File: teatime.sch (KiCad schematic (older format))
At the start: 85 parts, among them SW1 SW_Push, U1 MCP1700-3302E_TO92, U2 74HC595, U3 74HC595, U4 74HC595, U5 74HC595, U6 ATtiny85-20PU

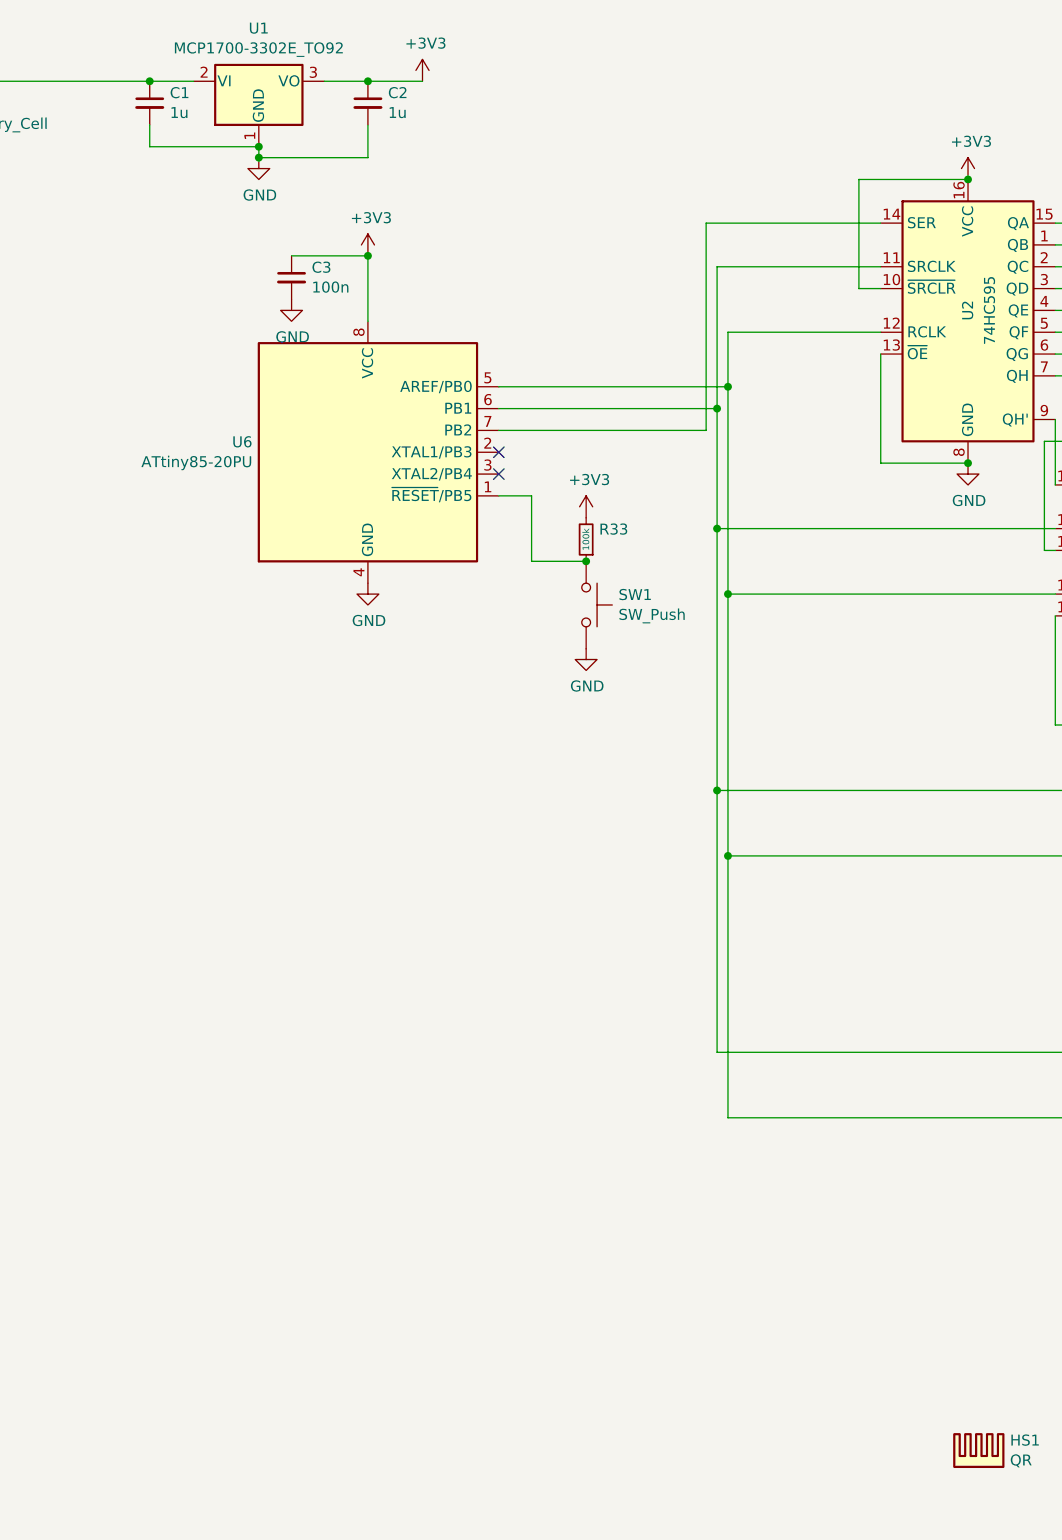
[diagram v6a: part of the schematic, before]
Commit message: More updates, added buzzer
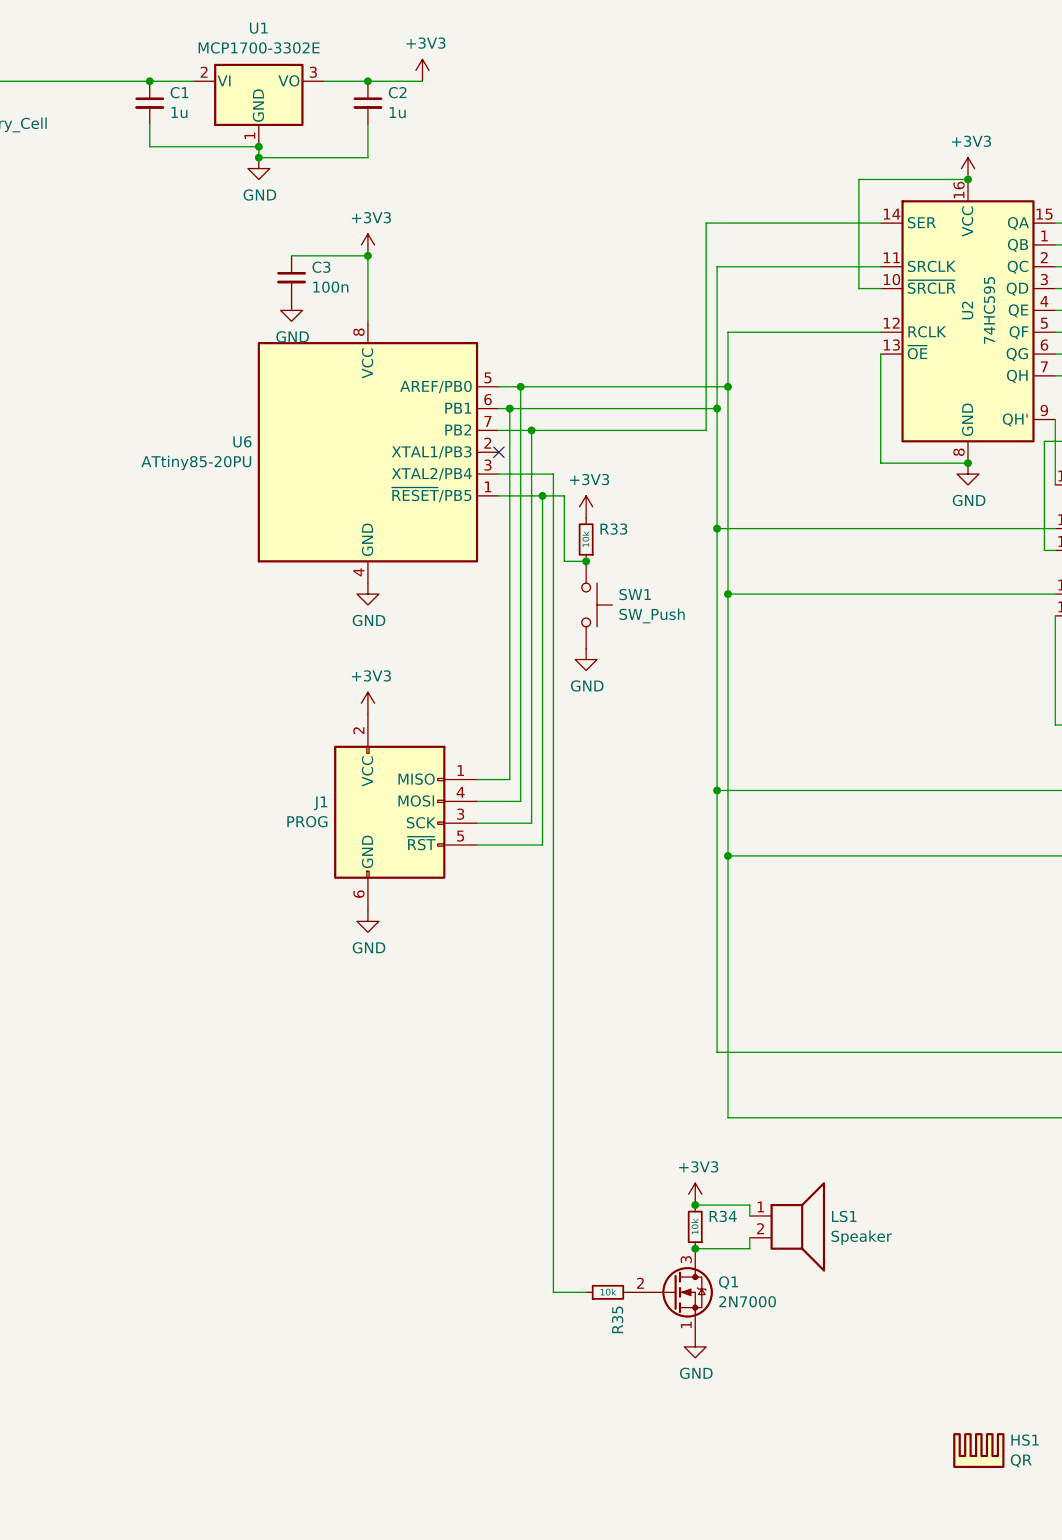
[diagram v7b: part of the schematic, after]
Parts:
- added J1: PROG, Connector_PinHeader_2.54mm:PinHeader_2x03_P2.54mm_Vertical, symbol Connector:AVR-ISP-6
- added LS1: Speaker, Buzzer_Beeper:Buzzer_12x9.5RM7.6, symbol Device:Speaker
- added Q1: 2N7000, Package_TO_SOT_THT:TO-92_Inline_W4.0mm_Horizontal_FlatSideDown, symbol Transistor_FET:2N7000
- added R34, R35: 10k, Resistor_THT:R_Axial_DIN0204_L3.6mm_D1.6mm_P7.62mm_Horizontal, symbol Device:R_Small
- R33: value 100k -> 10k
- U1: value MCP1700-3302E_TO92 -> MCP1700-3302E
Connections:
- net +3V3: now also J1.2 (VCC), LS1.1, R34.2
- net GND: now also J1.6 (GND), Q1.1 (S)
- net at U2.11 (SRCLK), U3.11 (SRCLK), U4.11 (SRCLK)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: now also J1.1 (MISO)
- net at U2.12 (RCLK), U3.12 (RCLK), U4.12 (RCLK)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: now also J1.4 (MOSI)
- net at U2.14 (SER), U6.7 (PB2): now also J1.3 (SCK)
- net at R33.1, SW1.1, U6.1 (~RESET~/PB5): now also J1.5 (~RST)
- net at U6.3 (XTAL2/PB4): now also R35.1
- new net: LS1.2, Q1.3 (D), R34.1
- new net: Q1.2 (G), R35.2
- no-connect marks 3 -> 2
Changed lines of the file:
@@
 P 3700 3000
 F 0 "R33" H 3641 2954 50  0000 R CNN
-F 1 "100k" V 3700 3000 30  0000 C CNN
+F 1 "10k" V 3700 3000 30  0000 C CNN
 F 2 "Resistor_THT:R_Axial_DIN0204_L3.6mm_D1.6mm_P7.62mm_Horizontal" H 3700 3000 50  0001 C CNN
 F 3 "~" H 3700 3000 50  0001 C CNN
@@
 $EndComp
 Wire Wire Line
-	3300 2800 3450 2800
-Wire Wire Line
-	3450 2800 3450 3100
-Wire Wire Line
-	3450 3100 3700 3100
+	3300 2800 3500 2800
+Wire Wire Line
+	3600 2800 3600 3100
+Wire Wire Line
+	3600 3100 3700 3100
 Connection ~ 3700 3100
 Wire Wire Line
-	3300 2400 4300 2400
+	3300 2400 3350 2400
 $Comp
 L Regulator_Linear:MCP1700-3302E_TO92 U1
@@
 P 2200 900
 F 0 "U1" H 2200 658 50  0000 C CNN
-F 1 "MCP1700-3302E_TO92" H 2200 749 50  0000 C CNN
+F 1 "MCP1700-3302E" H 2200 749 50  0000 C CNN
 F 2 "Package_TO_SOT_THT:TO-92_Inline_W4.0mm_Horizontal_FlatSideDown" H 2200 700 50  0001 C CIN
 F 3 "http://ww1.microchip.com/downloads/en/DeviceDoc/20001826D.pdf" H 2200 900 50  0001 C CNN
@@
 Connection ~ 2200 1200
 NoConn ~ 3300 2600
-NoConn ~ 3300 2700
 $Comp
 L Device:R_Small R2
@@
 	4350 2300 4350 3250
 Wire Wire Line
-	3300 2300 4350 2300
+	3300 2300 3400 2300
 Wire Wire Line
 	4250 1550 4250 2500
 Wire Wire Line
-	4250 2500 3300 2500
+	4250 2500 3450 2500
 Wire Wire Line
 	9050 1200 9400 1200
@@
 Connection ~ 700  900
 Connection ~ 700  1200
+$Comp
+L Connector:AVR-ISP-6 J1
+U 1 1 5E4866F5
+P 2800 4300
+F 0 "J1" H 2520 4396 50  0000 R CNN
+F 1 "PROG" H 2520 4305 50  0000 R CNN
+F 2 "Connector_PinHeader_2.54mm:PinHeader_2x03_P2.54mm_Vertical" V 2550 4350 50  0001 C CNN
+F 3 " ~" H 1525 3750 50  0001 C CNN
+	1    2800 4300
+	1    0    0    -1
+$EndComp
+$Comp
+L power:+3V3 #PWR0101
+U 1 1 5E4868CF
+P 2700 3800
+F 0 "#PWR0101" H 2700 3650 50  0001 C CNN
+F 1 "+3V3" H 2715 3973 50  0000 C CNN
+F 2 "" H 2700 3800 50  0001 C CNN
+F 3 "" H 2700 3800 50  0001 C CNN
+	1    2700 3800
+	1    0    0    -1
+$EndComp
+$Comp
+L power:GND #PWR0102
+U 1 1 5E486986
+P 2700 4700
+F 0 "#PWR0102" H 2700 4450 50  0001 C CNN
+F 1 "GND" H 2705 4527 50  0000 C CNN
+F 2 "" H 2700 4700 50  0001 C CNN
+F 3 "" H 2700 4700 50  0001 C CNN
+	1    2700 4700
+	1    0    0    -1
+$EndComp
+Wire Wire Line
+	3200 4100 3350 4100
+Wire Wire Line
+	3200 4200 3400 4200
+Wire Wire Line
+	3200 4300 3450 4300
+Wire Wire Line
+	3200 4400 3500 4400
+Wire Wire Line
+	3500 4400 3500 2800
+Connection ~ 3500 2800
+Wire Wire Line
+	3500 2800 3600 2800
+Wire Wire Line
+	3450 2500 3450 4300
+Connection ~ 3450 2500
+Wire Wire Line
+	3450 2500 3300 2500
+Wire Wire Line
+	3400 2300 3400 4200
+Connection ~ 3400 2300
+Wire Wire Line
+	3400 2300 4350 2300
+Wire Wire Line
+	3350 2400 3350 4100
+Connection ~ 3350 2400
+Wire Wire Line
+	3350 2400 4300 2400
+$Comp
+L Device:Speaker LS1
+U 1 1 5E4D2D09
+P 4650 6100
+F 0 "LS1" H 4820 6096 50  0000 L CNN
+F 1 "Speaker" H 4820 6005 50  0000 L CNN
+F 2 "Buzzer_Beeper:Buzzer_12x9.5RM7.6" H 4650 5900 50  0001 C CNN
+F 3 "~" H 4640 6050 50  0001 C CNN
+	1    4650 6100
+	1    0    0    -1
+$EndComp
+$Comp
+L Transistor_FET:2N7000 Q1
+U 1 1 5E4D2E2E
+P 4100 6450
+F 0 "Q1" H 4305 6496 50  0000 L CNN
+F 1 "2N7000" H 4305 6405 50  0000 L CNN
+F 2 "Package_TO_SOT_THT:TO-92_Inline_W4.0mm_Horizontal_FlatSideDown" H 4300 6375 50  0001 L CIN
+F 3 "https://www.fairchildsemi.com/datasheets/2N/2N7000.pdf" H 4100 6450 50  0001 L CNN
+	1    4100 6450
+	1    0    0    -1
+$EndComp
+$Comp
+L Device:R_Small R34
+U 1 1 5E4D2F24
+P 4200 6150
+F 0 "R34" H 4141 6104 50  0000 R CNN
+F 1 "10k" V 4200 6150 30  0000 C CNN
+F 2 "Resistor_THT:R_Axial_DIN0204_L3.6mm_D1.6mm_P7.62mm_Horizontal" H 4200 6150 50  0001 C CNN
+F 3 "~" H 4200 6150 50  0001 C CNN
+	1    4200 6150
+	-1   0    0    1
+$EndComp
+$Comp
+L Device:R_Small R35
+U 1 1 5E4D313D
+P 3800 6450
+F 0 "R35" H 3741 6404 50  0000 R CNN
+F 1 "10k" V 3800 6450 30  0000 C CNN
+F 2 "Resistor_THT:R_Axial_DIN0204_L3.6mm_D1.6mm_P7.62mm_Horizontal" H 3800 6450 50  0001 C CNN
+F 3 "~" H 3800 6450 50  0001 C CNN
+	1    3800 6450
+	0    -1   -1   0
+$EndComp
+Wire Wire Line
+	3300 2700 3550 2700
+$Comp
+L power:+3V3 #PWR021
+U 1 1 5E4E5E02
+P 4200 6050
+F 0 "#PWR021" H 4200 5900 50  0001 C CNN
+F 1 "+3V3" H 4215 6223 50  0000 C CNN
+F 2 "" H 4200 6050 50  0001 C CNN
+F 3 "" H 4200 6050 50  0001 C CNN
+	1    4200 6050
+	1    0    0    -1
+$EndComp
+Wire Wire Line
+	4450 6100 4450 6050
+Wire Wire Line
+	4450 6050 4200 6050
+Wire Wire Line
+	4450 6200 4450 6250
+Wire Wire Line
+	4450 6250 4200 6250
+Connection ~ 4200 6250
+Connection ~ 4200 6050
+$Comp
+L power:GND #PWR022
+U 1 1 5E502CAC
+P 4200 6650
+F 0 "#PWR022" H 4200 6400 50  0001 C CNN
+F 1 "GND" H 4205 6477 50  0000 C CNN
+F 2 "" H 4200 6650 50  0001 C CNN
+F 3 "" H 4200 6650 50  0001 C CNN
+	1    4200 6650
+	1    0    0    -1
+$EndComp
+Wire Wire Line
+	3550 6450 3700 6450
+Wire Wire Line
+	3550 2700 3550 6450
 $EndSCHEMATC
